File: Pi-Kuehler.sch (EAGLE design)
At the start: 14 parts, among them IC1 ATTINY85-20S, Q1 BC847ASMD, X1 MAC64L, X2 FAN

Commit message: Schaltpläne optimiert
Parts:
- R1: value 330 -> 1k2
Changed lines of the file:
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@@
 </classes>
 <parts>
-<part name="R1" library="rcl" deviceset="R-EU_" device="R1206" value="330"/>
+<part name="R1" library="rcl" deviceset="R-EU_" device="R1206" value="1k2"/>
 <part name="LED1" library="led" deviceset="LED" device="CHIPLED_1206" value="2mA bl"/>
 <part name="X1" library="con-vg" deviceset="MAC64L" device=""/>

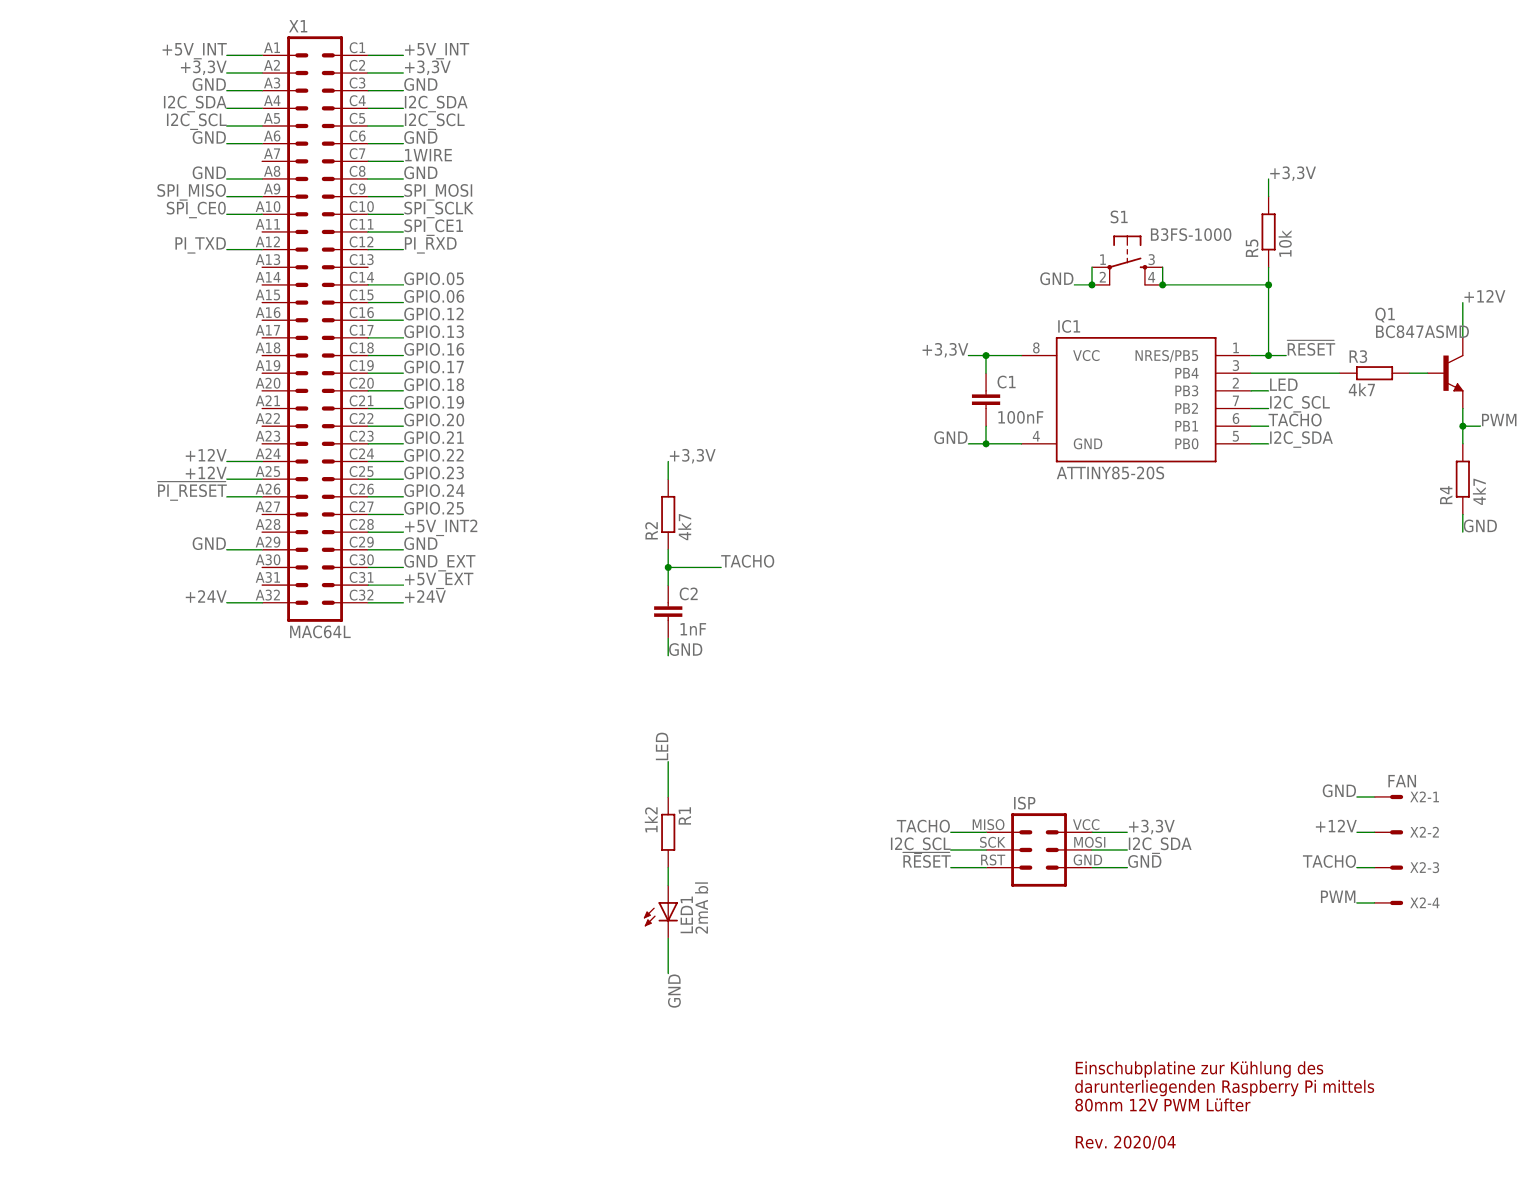
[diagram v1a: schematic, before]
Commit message: Readme und Lizenz aktualisiert, Schaltpläne optimiert
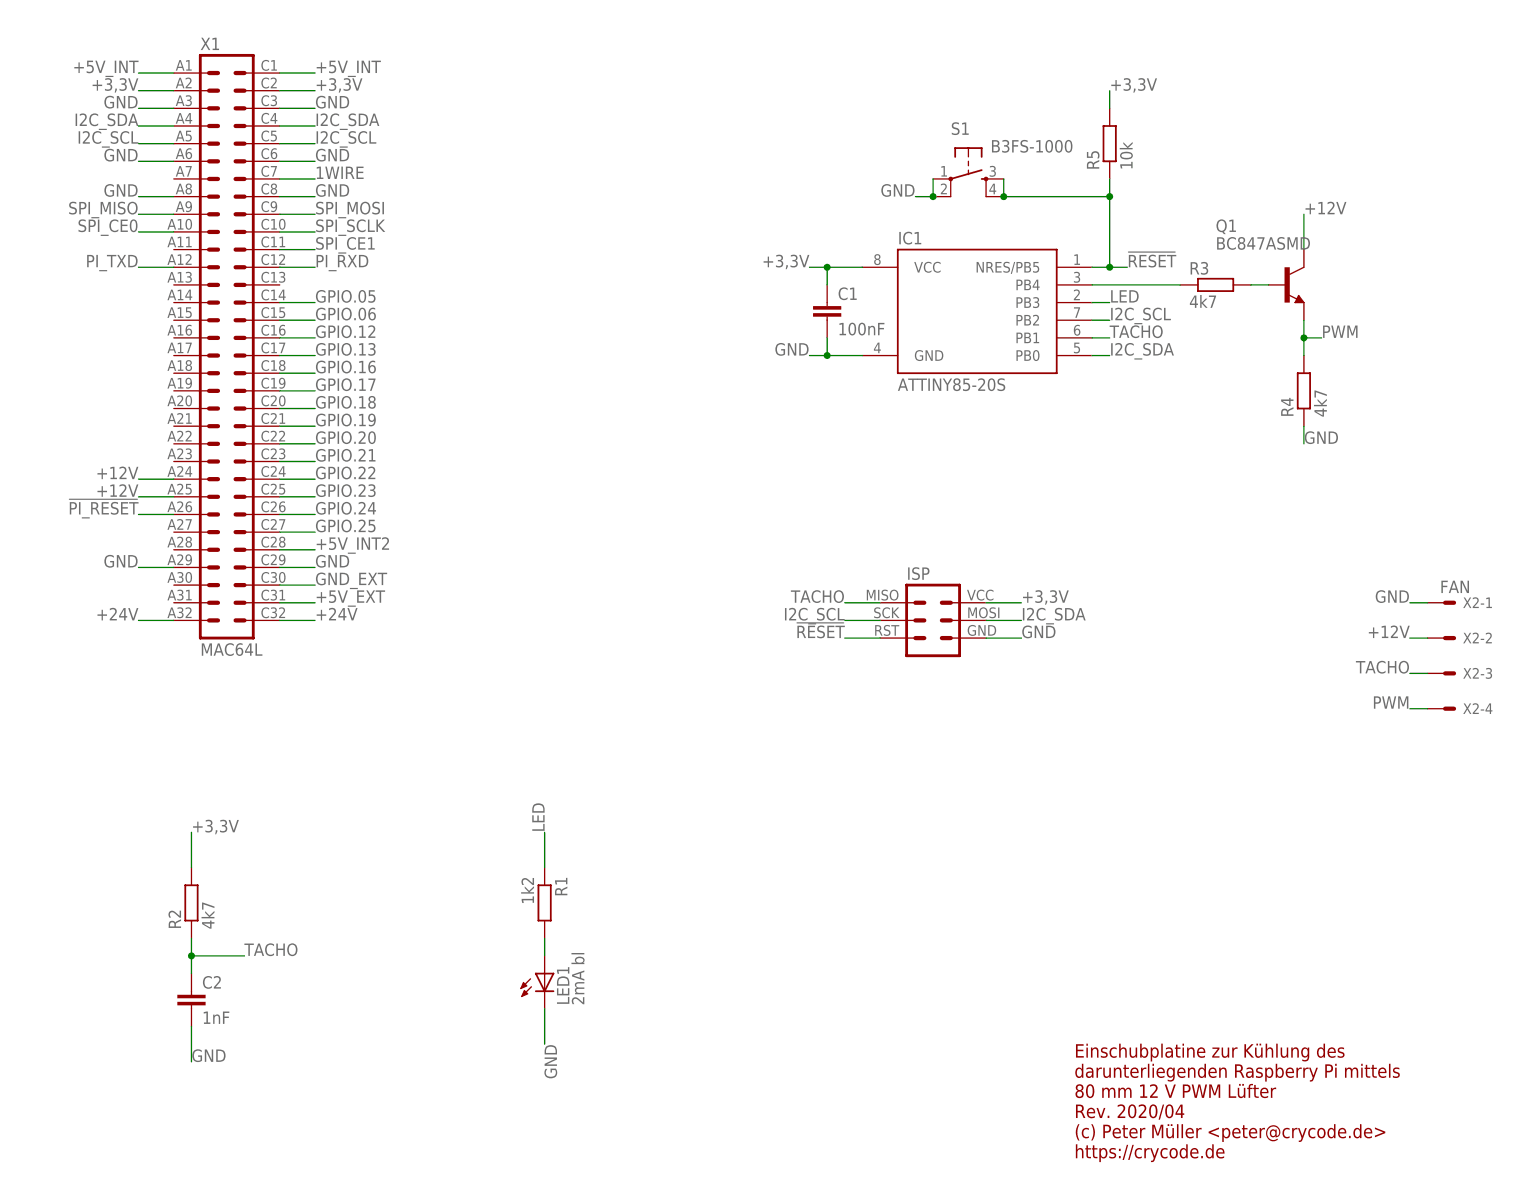
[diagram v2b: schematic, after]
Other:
- note added: "Einschubplatine zur Kühlung des darunterliegenden Raspberry Pi mittels 80 mm 12 V PWM Lüfter Rev. 2020/04 (c) Peter Müller <peter@crycode.de> https://crycode.de"
- note removed: "Einschubplatine zur Kühlung des darunterliegenden Raspberry Pi mittels 80mm 12V PWM Lüfter Rev. 2020/04"
- moved on the sheet: C1, C2, IC1, ISP, LED1, Q1, R1, R2, R3, R4, R5, S1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
